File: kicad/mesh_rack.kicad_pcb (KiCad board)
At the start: 4 copper layers, 200 x 100 mm, 86 parts, among them J1 Input, J10 Conn_01x02, J11 Conn_01x04, J12 Conn_Coaxial_Small, J2 Power Switch, J3 USB_C_Receptacle_USB2.0_14P, J4 Conn_01x02, J5 BOOT, J6 EN, J7 Conn_Coaxial_Small, J8 Conn_02x09_Counter_Clockwise, J9 Conn_01x10, Q1 IRF9540N, Q2 IRF540N, U1 NEO-M8N, U2 ESP32-S3-WROOM-1, U3 LM22678TJ-5, U4 LM2596S-3.3, U5 TPD2EUSB30, U6 E22-900M30S, U7 INA260

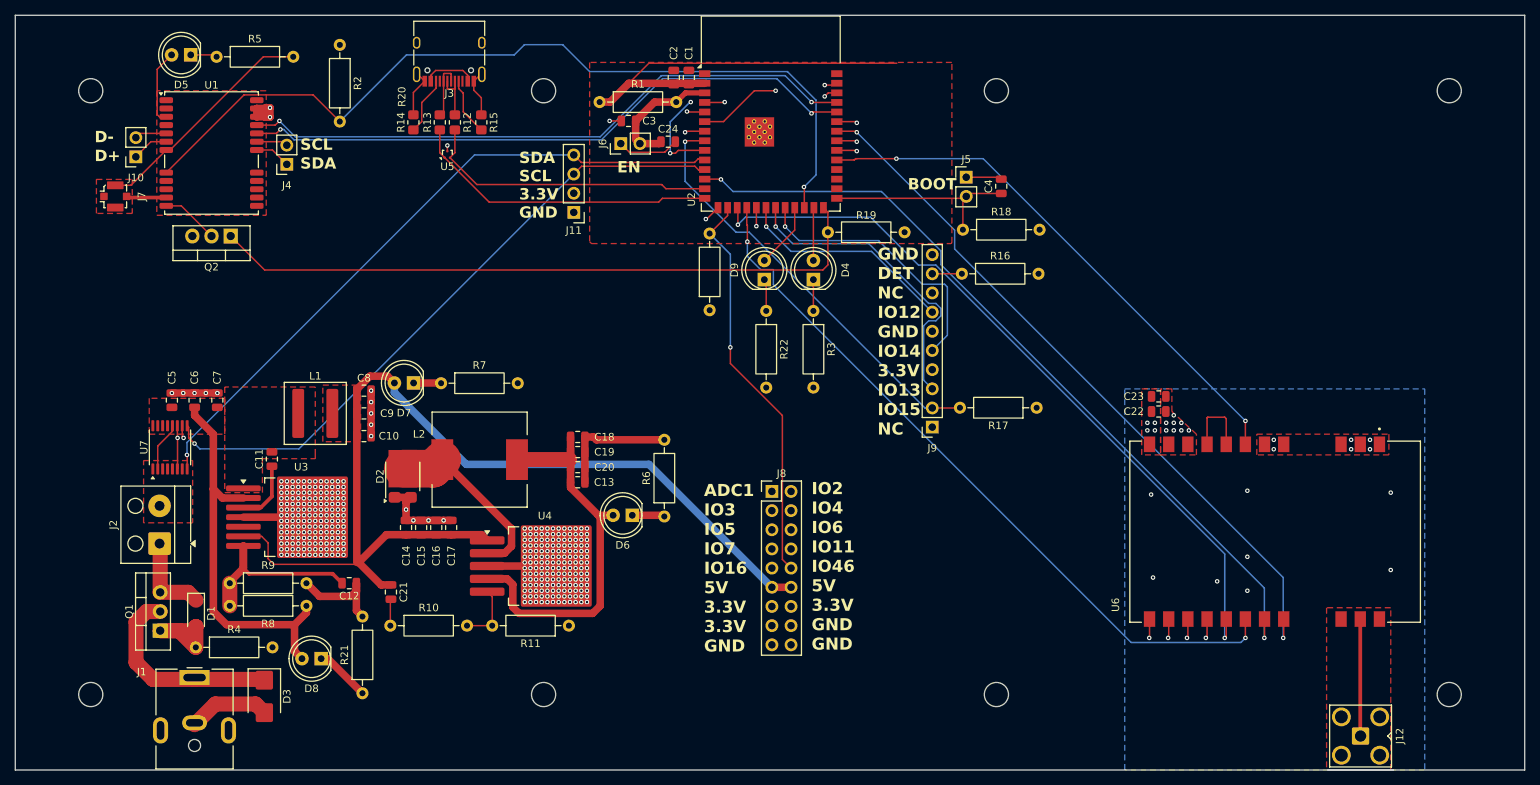
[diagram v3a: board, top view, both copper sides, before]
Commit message: make bom cheaper by using through hole parts
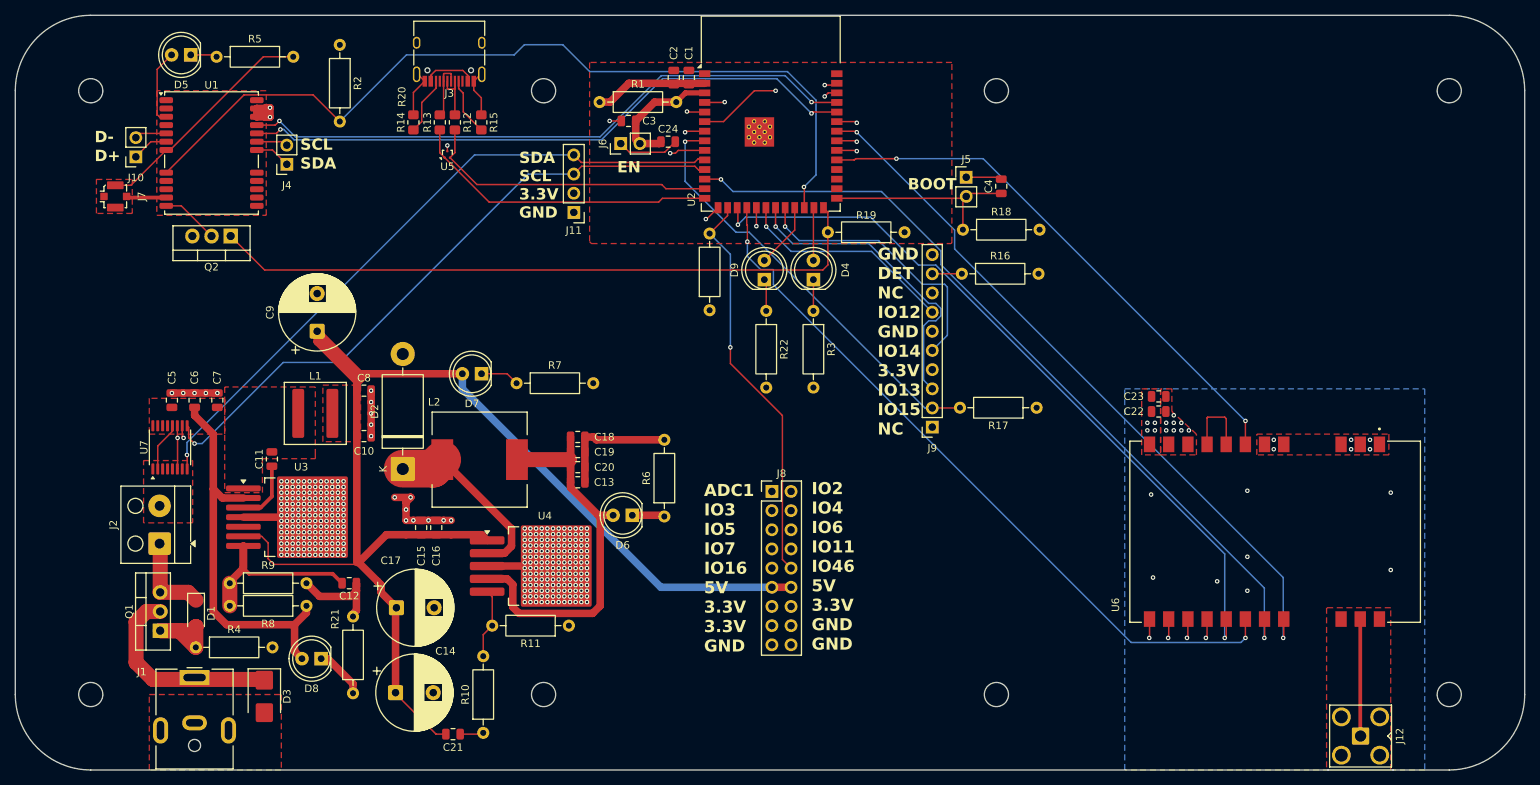
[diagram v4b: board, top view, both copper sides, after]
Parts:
- C14, C17, C9: footprint Capacitor_SMD:C_0805_2012Metric -> Capacitor_THT:CP_Radial_D10.0mm_P5.00mm
- D2: value PMEG030V050EPD -> SB5H90; footprint Package_TO_SOT_SMD:Nexperia_CFP15_SOT-1289 -> Diode_THT:D_DO-201AD_P15.24mm_Horizontal
- moved C14 21.9 mm to (75.4, 114.8), turned to 0 degrees
- moved C21 20.5 mm to (83.0, 120.2), turned to 0 degrees
- moved R10 18.8 mm to (87.0, 120.1), turned to 90 degrees
- moved C17 12.9 mm to (75.5, 103.5), turned to 0 degrees
- moved C9 12.5 mm to (65.0, 66.9), turned to 90 degrees
- moved R7 10.0 mm to (91.4, 73.8)
- moved D7 9.08 mm to (86.8, 72.5)
- moved R21 1.25 mm to (69.8, 114.8)
- moved D2 0.97 mm to (76.3, 85.1)
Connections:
- D2 pad 1: GND -> Net-(D2-K)
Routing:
- net +5V: track 136.0 -> 178.0 mm
- net +3.3V: track 116.7 -> 80.1 mm
- net GND: track 149.8 -> 138.8 mm, vias 372 -> 376
- net /ESP32/IO16: track 75.6 -> 67.7 mm, vias 2 -> 1
- net Net-(D7-K): track 3.66 -> 5.16 mm
- net Net-(U4-~{ON}/OFF): track 8.12 -> 9.32 mm
- net SCL: track 86.4 -> 85.8 mm
- net Net-(D8-K): track 7.37 -> 6.85 mm
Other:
- outline, holes or cut-outs redrawn

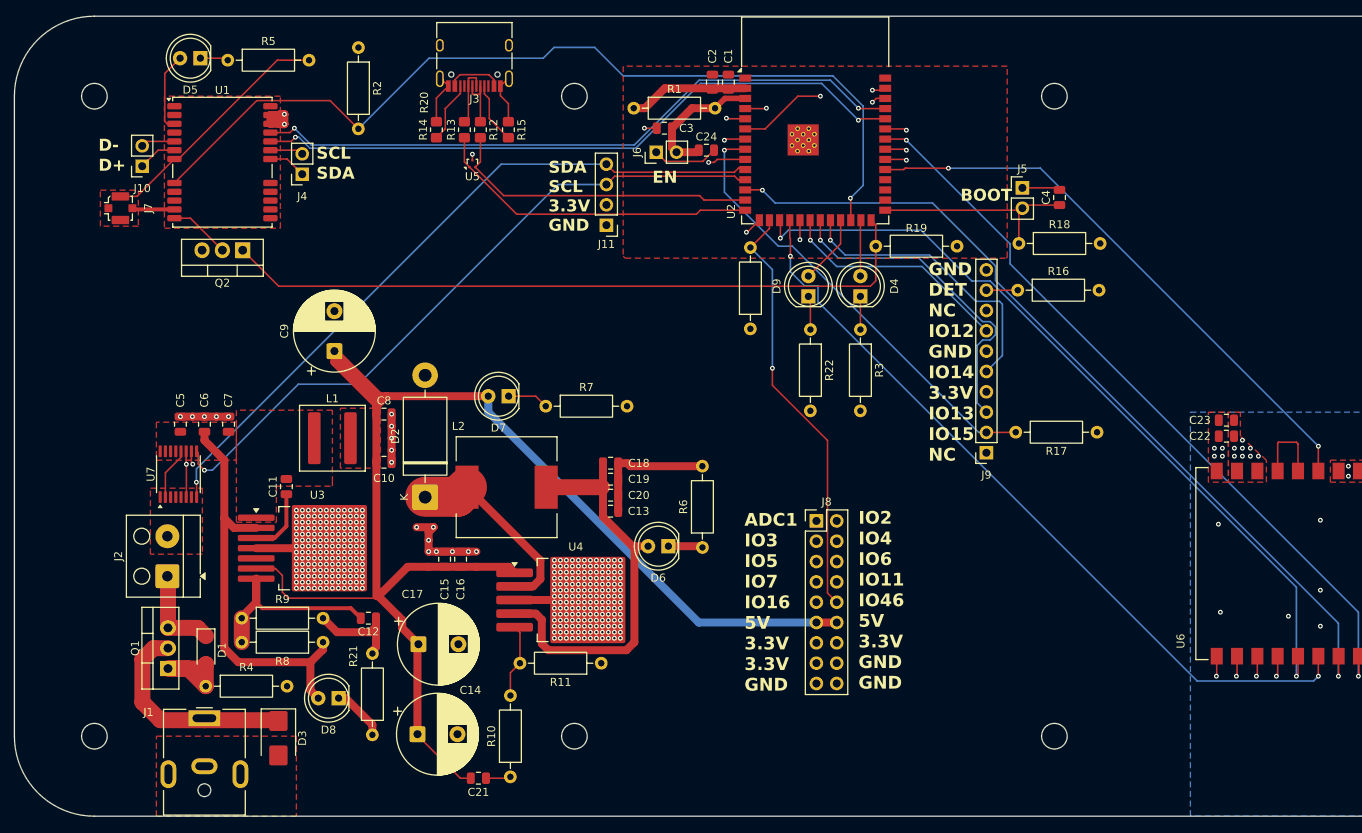
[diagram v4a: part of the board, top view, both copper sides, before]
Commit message: make bom cheaper
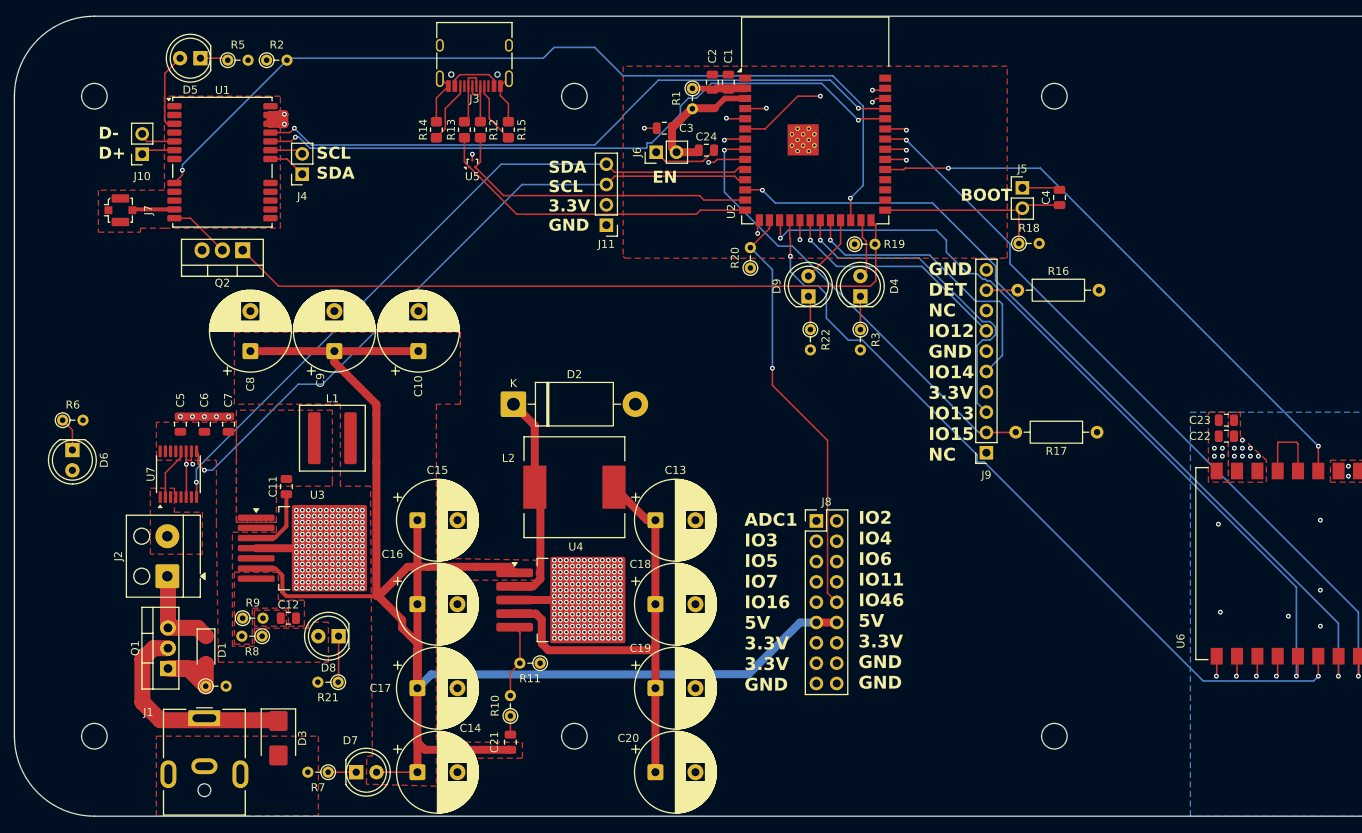
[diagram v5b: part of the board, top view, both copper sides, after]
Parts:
- C10, C13, C15, C16, C18, C19, C20, C8: footprint Capacitor_SMD:C_0805_2012Metric -> Capacitor_THT:CP_Radial_D10.0mm_P5.00mm
- R1, R10, R11, R18, R19, R2, R20, R22, R3, R4, R5, R6, R7, R8, R9: footprint Resistor_THT:R_Axial_DIN0207_L6.3mm_D2.5mm_P10.16mm_Horizontal -> Resistor_THT:R_Axial_DIN0204_L3.6mm_D1.6mm_P2.54mm_Vertical
- R21: value 10k -> 100k; footprint Resistor_THT:R_Axial_DIN0207_L6.3mm_D2.5mm_P10.16mm_Horizontal -> Resistor_THT:R_Axial_DIN0204_L3.6mm_D1.6mm_P2.54mm_Vertical
- moved R6 81.5 mm to (31.0, 75.5), turned to 0 degrees
- moved D6 75.5 mm to (32.2, 79.2), turned to -90 degrees
- moved R7 53.2 mm to (64.2, 119.5), turned to 180 degrees
- moved D7 50.7 mm to (67.7, 119.5), turned to 0 degrees
- moved C20 35.1 mm to (105.1, 119.5)
- moved C19 26.7 mm to (105.1, 109.0)
- moved C18 18.5 mm to (105.1, 98.5)
- moved C8 18.5 mm to (54.5, 66.9), turned to 90 degrees
- moved D2 16.0 mm to (87.4, 73.5), turned to 0 degrees
- moved C10 14.5 mm to (75.5, 66.9), turned to 90 degrees
- moved R19 12.8 mm to (130.0, 53.5), turned to 0 degrees
- moved R2 11.6 mm to (56.5, 30.5), turned to 0 degrees
- moved C12 10.0 mm to (59.2, 100.2), turned to 0 degrees
- moved L2 8.47 mm to (95.0, 83.9)
- moved R21 7.85 mm to (65.5, 108.2), turned to 180 degrees
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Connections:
- J7 pad 2: GND -> GPS_GND
- Q2 pad 2: Net-(Q2-D) -> GPS_GND
- U1 pad 10: Net-(Q2-D) -> GPS_GND
- U1 pad 12: Net-(Q2-D) -> GPS_GND
- U1 pad 13: Net-(Q2-D) -> GPS_GND
- U1 pad 24: Net-(Q2-D) -> GPS_GND
- U1 pad 7: GND -> GPS_GND
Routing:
- net GND: track 138.8 -> 60.8 mm, vias 376 -> 363
- net /Power Input/RAW: track 52.1 -> 0.00 mm
- net +5V: track 178.0 -> 213.2 mm
- net Net-(U3-EN): track 25.5 -> 0.00 mm
- net Net-(Q2-D): track 7.66 -> 0.00 mm
- net GPS_GND: track 0.00 -> 7.66 mm
- net Net-(D2-K): track 24.6 -> 26.9 mm
- net /ESP32/IO47: track 114.0 -> 111.8 mm, vias 1 -> 2
- net Net-(D7-K): track 5.16 -> 3.50 mm
- net +3.3V: track 80.1 -> 78.7 mm
- net /ESP32/IO3: track 44.6 -> 43.3 mm
- net /ESP32/LORA_MOSI: track 97.6 -> 98.7 mm
- net /ESP32/MCU_RXD0: track 83.0 -> 83.9 mm
- net /ESP32/LORA_MISO: track 99.4 -> 100.3 mm
- net Net-(C21-Pad2): track 3.12 -> 2.33 mm
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- added copper zone on F.Cu, net GPS_GND
- added copper zone on F.Cu, net Net-(U3-EN)
- removed copper zone on F.Cu, net Net-(Q2-D)

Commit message: update
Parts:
- C1, C23, C3: footprint Capacitor_SMD:C_0805_2012Metric -> Capacitor_THT:CP_Radial_D5.0mm_P2.50mm
- J1: footprint Connector_BarrelJack:BarrelJack_CUI_PJ-063AH_Horizontal -> Connector_BarrelJack:BarrelJack_Horizontal
- moved C1 9.08 mm to (105.2, 34.0), turned to 180 degrees
- moved C3 7.32 mm to (105.2, 46.2)
- moved C23 4.02 mm to (178.0, 71.8)
- moved R4 3.79 mm to (52.3, 107.0)
- moved J6 3.54 mm to (102.7, 39.5)
- moved J1 1.66 mm to (48.0, 111.2), turned to 90 degrees
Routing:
- net GND: track 60.8 -> 50.9 mm, vias 363 -> 362
- net Net-(J6-Pin_2): track 16.8 -> 25.8 mm
- net Net-(D1-A): track 13.4 -> 17.0 mm
- net Net-(D3-A1): track 27.1 -> 25.6 mm

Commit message: updadte
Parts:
- removed C21: 0.1uF, Capacitor_SMD:C_0805_2012Metric
- removed R10, R11: 47k, Resistor_THT:R_Axial_DIN0204_L3.6mm_D1.6mm_P2.54mm_Vertical
- removed R8: 100k, Resistor_THT:R_Axial_DIN0204_L3.6mm_D1.6mm_P2.54mm_Vertical
- removed R9: 18k, Resistor_THT:R_Axial_DIN0204_L3.6mm_D1.6mm_P2.54mm_Vertical
- added D10: 1N5820, Diode_THT:D_DO-201AD_P15.24mm_Horizontal, F.Cu at (55.8, 83.8)
- C11, C22: footprint Capacitor_SMD:C_0805_2012Metric -> Capacitor_THT:C_Disc_D5.0mm_W2.5mm_P5.00mm
- C12: value 100nF -> 10uF; footprint Capacitor_SMD:C_0805_2012Metric -> Capacitor_THT:CP_Radial_D5.0mm_P2.50mm
- C5, C6, C7: footprint Capacitor_SMD:C_0805_2012Metric -> Capacitor_THT:CP_Radial_D10.0mm_P5.00mm
- D2: value SB5H90 -> 1N5820
- L1: value 10uH Coilcraft XAL7030-103 -> 33uH; footprint Inductor_SMD:L_Coilcraft_XAL7030-103 -> Inductor_SMD:L_1206_3216Metric
- L2: value 22uH -> 47uH; footprint Inductor_SMD:L_12x12mm_H4.5mm -> Inductor_SMD:L_1206_3216Metric
- U3: value LM22678TJ-5 -> XL1509-5.0; footprint Package_TO_SOT_SMD:TO-263-7_TabPin8 -> Package_SO:SOIC-8_3.9x4.9mm_P1.27mm
- U4: value LM2596S-3.3 -> XL1509-3.3; footprint Package_TO_SOT_SMD:TO-263-5_TabPin3 -> Package_SO:SOIC-8_3.9x4.9mm_P1.27mm
- moved C12 64.6 mm to (68.0, 36.2), turned to 90 degrees
- moved C11 46.4 mm to (62.0, 37.5)
- moved L2 3.62 mm to (92.5, 86.5)
- moved U3 1.62 mm to (64.5, 91.5)
- moved U4 1.58 mm to (96.8, 98.0)
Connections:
- C11 pad 1: Net-(U3-BOOT) -> +3.3V
- C11 pad 2: Net-(U3-SW) -> GND
- C12 pad 1: GND -> +3.3V
- C12 pad 2: Net-(U3-EN) -> GND
- L1 pad 1: Net-(U3-SW) -> Net-(D10-K)
- U3 pad 1: Net-(U3-SW) -> /Power Input/RAW
- U3 pad 2: /Power Input/RAW -> Net-(D10-K)
- U3 pad 3: Net-(U3-BOOT) -> +5V
- U3 pad 4: GND -> /Power Input/RAW
- U3 pad 5: unconnected-(U3-NC-Pad5) -> GND
- U3 pad 6: +5V -> GND
- U3 pad 7: Net-(U3-EN) -> GND
- U4 pad 3: GND -> +3.3V
- U4 pad 4: +3.3V -> +5V
- U4 pad 5: Net-(U4-~{ON}/OFF) -> GND
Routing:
- net GND: track 50.9 -> 32.6 mm, vias 362 -> 34
- net +5V: track 213.2 -> 195.6 mm
- net Net-(U4-~{ON}/OFF): track 9.32 -> 0.00 mm
- net Net-(U3-BOOT): track 8.39 -> 0.00 mm
- net +3.3V: track 78.7 -> 86.5 mm
- net Net-(D2-K): track 26.9 -> 29.9 mm
- net Net-(C21-Pad2): track 2.33 -> 0.00 mm
- added copper zone on F.Cu, net Net-(D10-K)
- removed copper zone on F.Cu, net Net-(U3-EN)
- removed copper zone on F.Cu, net Net-(U3-SW)

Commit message: update pcb
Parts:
- added JP1: SolderJumper_2_Open, Jumper:SolderJumper-2_P1.3mm_Open_RoundedPad1.0x1.5mm, F.Cu at (41.2, 82.2)
- moved D6 23.5 mm to (33.8, 102.7)
- moved R6 23.5 mm to (32.5, 99.0)
- moved C7 22.1 mm to (37.1, 59.5), turned to 180 degrees
- moved C6 13.1 mm to (37.1, 70.0), turned to 180 degrees
- moved C5 9.73 mm to (37.1, 80.5), turned to 180 degrees
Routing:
- net GND: track 32.6 -> 26.6 mm, vias 34 -> 29
